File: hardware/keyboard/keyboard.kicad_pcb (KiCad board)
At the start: 2 copper layers, 80.3 x 73.7 mm, 24 parts, among them J1 Conn_01x06, SW1 SW_PUSH, SW2 SW_PUSH, SW3 SW_PUSH, SW4 SW_PUSH, SW5 SW_PUSH, SW6 SW_PUSH, SW7 SW_PUSH, SW8 SW_PUSH, SW9 SW_PUSH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

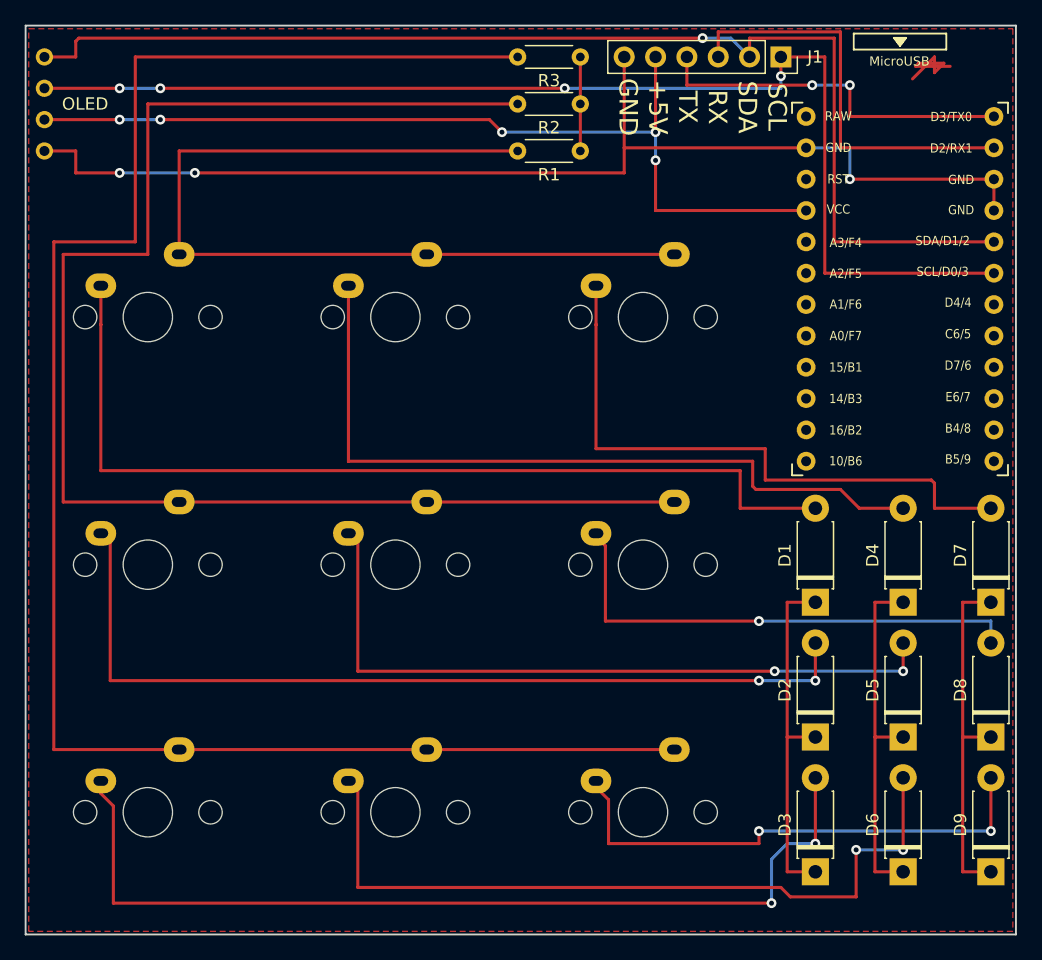
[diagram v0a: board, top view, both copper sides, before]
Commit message: Update ProMicro footprint
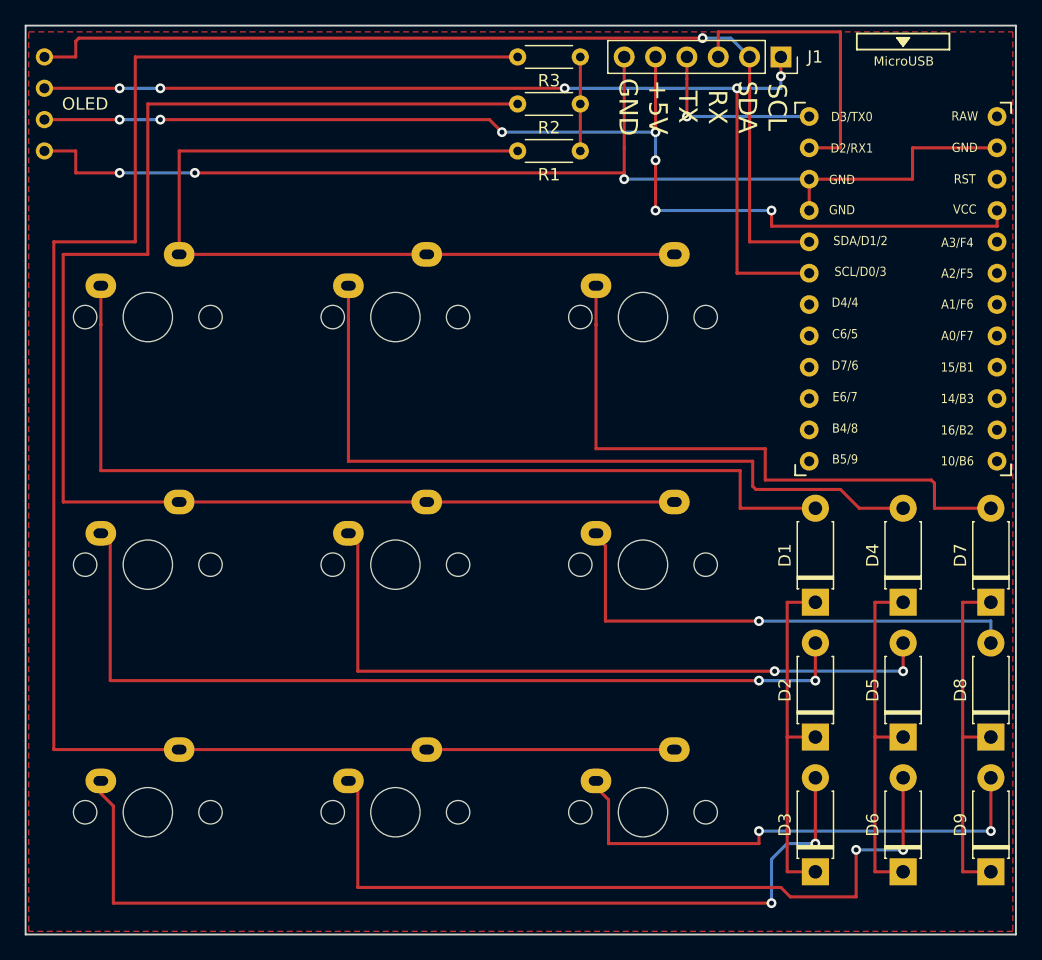
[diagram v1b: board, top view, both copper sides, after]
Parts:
- U1: footprint kbd:ProMicro_v3 -> arduino:ProMicro_v3
- moved U1 1.30 mm to (168.4, 87.1)
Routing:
- net +5V: track 74.6 -> 92.6 mm, vias 5 -> 7
- net Net-(J1-Pad2): track 97.0 -> 79.0 mm
- net Net-(J1-Pad4): track 29.7 -> 14.7 mm, vias 2 -> 1
- net Net-(J1-Pad1): track 97.0 -> 83.1 mm, vias 4 -> 5
- net (no net): track 10.0 -> 0.00 mm
- net Net-(J1-Pad3): track 33.8 -> 23.9 mm
- net GND: track 93.2 -> 94.0 mm
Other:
- board text added: "Keypad Prototype; REV1.1 nnarain"
- board text removed: "Keypad Prototype; REV1 nnarain"
